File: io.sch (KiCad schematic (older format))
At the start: 12 parts, among them X1 CON-JST_SM04B-SRSS-TB, X2 CON-JST_SM04B-SRSS-TB, X3 CON-JST_SM04B-SRSS-TB, X4 CON-JST_SM04B-SRSS-TB, X5 CON-JST_SM04B-SRSS-TB, X6 CON-JST_SM04B-SRSS-TB, X7 CON-JST_SM04B-SRSS-TB, X8 CON-JST_SM04B-SRSS-TB

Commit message: added lots of stuff
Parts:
- added R8: 2k, Resistors_SMD:R_0402, symbol R
- R4: value 0R -> 10k
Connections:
- net GND: now also R8.2
- net TX2/ADC123_IN2: now also R8.1
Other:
- moved on the sheet: R4
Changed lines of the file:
@@
 EESchema Schematic File Version 2
+LIBS:stm32f4_lqfp64_mpu6050-rescue
 LIBS:power
 LIBS:device
@@
 LIBS:minimal
 LIBS:alis_parts
+LIBS:sensors
+LIBS:stm32
 LIBS:stm32f4_lqfp64_mpu6050-cache
 EELAYER 25 0
@@
 $Descr A4 11693 8268
 encoding utf-8
-Sheet 2 7
+Sheet 2 10
 Title ""
 Date ""
@@
 $EndComp
 $Comp
-L GND #PWR6
+L GND #PWR20
 U 1 1 5699735E
 P 7650 3350
-F 0 "#PWR6" H 7650 3100 50  0001 C CNN
+F 0 "#PWR20" H 7650 3100 50  0001 C CNN
 F 1 "GND" H 7658 3176 50  0000 C CNN
 F 2 "" H 7650 3350 50  0000 C CNN
@@
 TX5
 $Comp
-L GND #PWR4
+L GND #PWR9
 U 1 1 56997382
 P 4800 2850
-F 0 "#PWR4" H 4800 2600 50  0001 C CNN
+F 0 "#PWR9" H 4800 2600 50  0001 C CNN
 F 1 "GND" H 4808 2676 50  0000 C CNN
 F 2 "" H 4800 2850 50  0000 C CNN
@@
 TX4
 $Comp
-L GND #PWR8
+L GND #PWR26
 U 1 1 569973A7
 P 6300 4050
-F 0 "#PWR8" H 6300 3800 50  0001 C CNN
+F 0 "#PWR26" H 6300 3800 50  0001 C CNN
 F 1 "GND" H 6308 3876 50  0000 C CNN
 F 2 "" H 6300 4050 50  0000 C CNN
@@
 TX3
 $Comp
-L GND #PWR7
+L GND #PWR25
 U 1 1 569973CC
 P 3500 4050
-F 0 "#PWR7" H 3500 3800 50  0001 C CNN
+F 0 "#PWR25" H 3500 3800 50  0001 C CNN
 F 1 "GND" H 3508 3876 50  0000 C CNN
 F 2 "" H 3500 4050 50  0000 C CNN
@@
 $EndComp
 $Comp
-L GND #PWR5
+L GND #PWR10
 U 1 1 569973EE
 P 6350 2850
-F 0 "#PWR5" H 6350 2600 50  0001 C CNN
+F 0 "#PWR10" H 6350 2600 50  0001 C CNN
 F 1 "GND" H 6358 2676 50  0000 C CNN
 F 2 "" H 6350 2850 50  0000 C CNN
@@
 TX1
 $Comp
-L GND #PWR3
+L GND #PWR8
 U 1 1 56997413
 P 3500 2850
-F 0 "#PWR3" H 3500 2600 50  0001 C CNN
+F 0 "#PWR8" H 3500 2600 50  0001 C CNN
 F 1 "GND" H 3508 2676 50  0000 C CNN
 F 2 "" H 3500 2850 50  0000 C CNN
@@
 $EndComp
 $Comp
-L GND #PWR2
+L GND #PWR4
 U 1 1 569B0BD9
 P 3550 2100
-F 0 "#PWR2" H 3550 1850 50  0001 C CNN
+F 0 "#PWR4" H 3550 1850 50  0001 C CNN
 F 1 "GND" H 3558 1926 50  0000 C CNN
 F 2 "" H 3550 2100 50  0000 C CNN
@@
 L R R4
 U 1 1 569BB569
-P 7150 1950
-F 0 "R4" H 7220 1996 50  0000 L CNN
-F 1 "0R" H 7220 1904 50  0000 L CNN
-F 2 "Resistors_SMD:R_0402" V 7080 1950 50  0001 C CNN
-F 3 "" H 7150 1950 50  0000 C CNN
-	1    7150 1950
-	0    1    1    0
-$EndComp
-Text GLabel 7000 1950 0    60   Input ~ 0
+P 7050 1400
+F 0 "R4" H 7120 1446 50  0000 L CNN
+F 1 "10k" H 7120 1354 50  0000 L CNN
+F 2 "Resistors_SMD:R_0402" V 6980 1400 50  0001 C CNN
+F 3 "" H 7050 1400 50  0000 C CNN
+	1    7050 1400
+	1    0    0    -1
+$EndComp
+Text GLabel 7200 1600 2    60   Input ~ 0
 TX2/ADC123_IN2
-Text GLabel 7300 1950 2    60   Input ~ 0
+Text GLabel 7050 1100 0    60   Input ~ 0
 VCCEXT
+$Comp
+L R R8
+U 1 1 569D6AA2
+P 7050 1800
+F 0 "R8" H 7120 1846 50  0000 L CNN
+F 1 "2k" H 7120 1754 50  0000 L CNN
+F 2 "Resistors_SMD:R_0402" V 6980 1800 50  0001 C CNN
+F 3 "" H 7050 1800 50  0000 C CNN
+	1    7050 1800
+	1    0    0    -1
+$EndComp
+$Comp
+L GND #PWR5
+U 1 1 569D6B3D
+P 7050 2100
+F 0 "#PWR5" H 7050 1850 50  0001 C CNN
+F 1 "GND" H 7058 1926 50  0000 C CNN
+F 2 "" H 7050 2100 50  0000 C CNN
+F 3 "" H 7050 2100 50  0000 C CNN
+	1    7050 2100
+	1    0    0    -1
+$EndComp
+Wire Wire Line
+	7050 1100 7050 1250
+Wire Wire Line
+	7050 1550 7050 1650
+Wire Wire Line
+	7200 1600 7050 1600
+Connection ~ 7050 1600
+Wire Wire Line
+	7050 1950 7050 2100
 $EndSCHEMATC

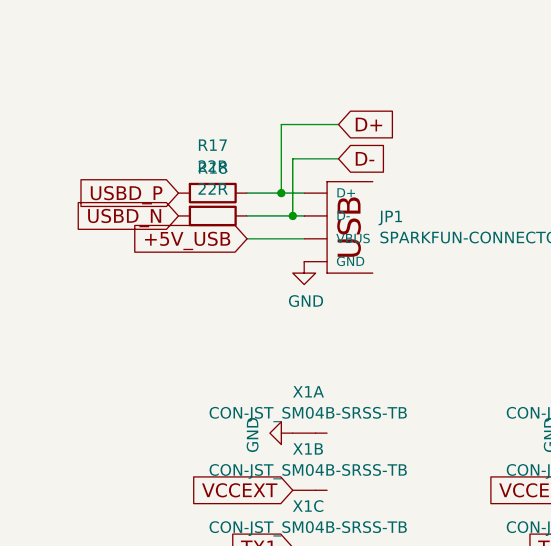
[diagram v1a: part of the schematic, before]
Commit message: added IMU int and USB sense in schematic
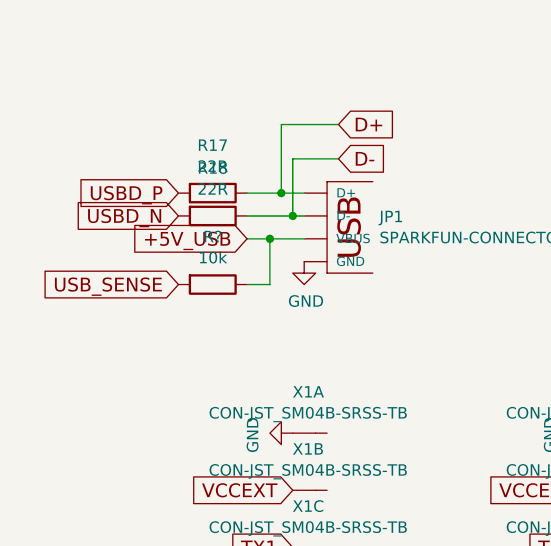
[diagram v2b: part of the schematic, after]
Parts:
- added R?: 10k, Resistors_SMD:R_0402, symbol R
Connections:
- net +5V_USB: now also R?.1
- new net USB_SENSE: R?.2
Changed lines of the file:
@@
 Wire Wire Line
 	7050 1950 7050 2100
+$Comp
+L R R?
+U 1 1 57056D51
+P 3150 2200
+F 0 "R?" V 2942 2200 50  0000 C CNN
+F 1 "10k" V 3034 2200 50  0000 C CNN
+F 2 "Resistors_SMD:R_0402" V 3080 2200 50  0001 C CNN
+F 3 "" H 3150 2200 50  0000 C CNN
+	1    3150 2200
+	0    1    1    0
+$EndComp
+Wire Wire Line
+	3300 2200 3400 2200
+Wire Wire Line
+	3400 2200 3400 2000
+Connection ~ 3400 2000
+Text GLabel 3000 2200 0    60   Input ~ 0
+USB_SENSE
 $EndSCHEMATC

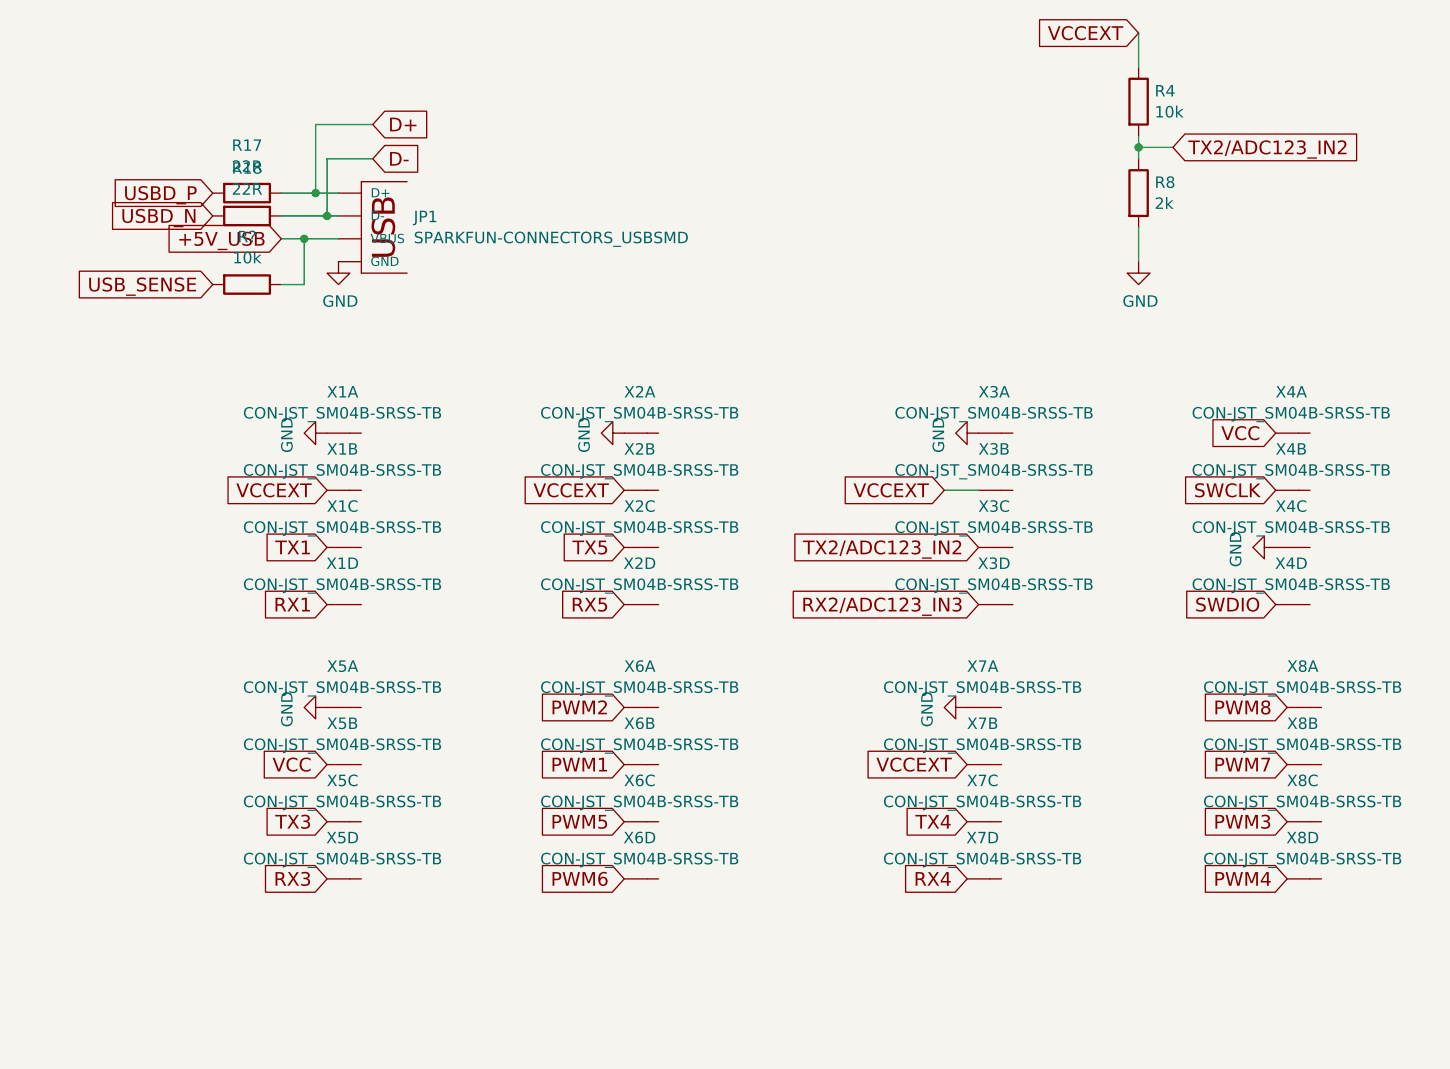
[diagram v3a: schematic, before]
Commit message: changed some netnames
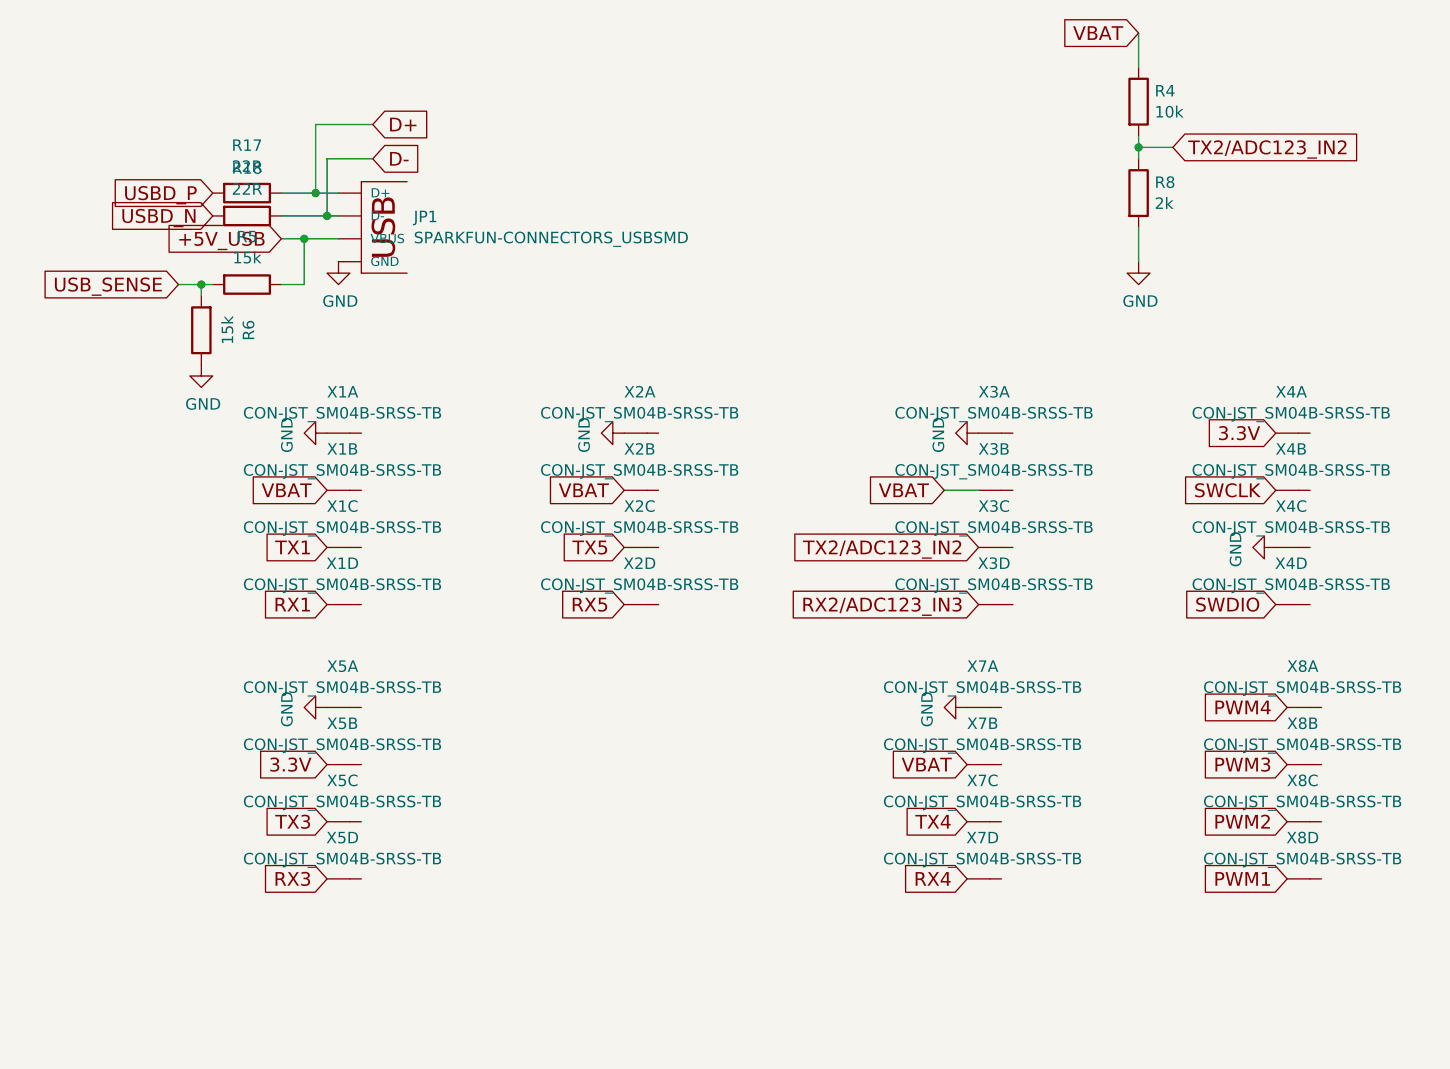
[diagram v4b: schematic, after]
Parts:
- removed X6: CON-JST_SM04B-SRSS-TB, Connectors_JST_SH:Connectors_JST_SM04B-SRSS-TB, symbol CON-JST_SM04B-SRSS-TB
- added R6: 15k, Resistors_SMD:R_0402, symbol R
- R5: renamed from R?; value 10k -> 15k
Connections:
- net PWM7 is gone; now on net PWM3: X8.2 (S)
- net PWM8 is gone; now on net PWM4: X8.1 (S)
- net GND: now also R6.1
- net PWM1: now also X8.4 (S)
- net PWM2: now also X8.3 (S)
- net PWM3: no longer X8.3 (S)
- net PWM4: no longer X8.4 (S)
- net USB_SENSE: now also R6.2
- net VCC renamed 3.3V
- net VCCEXT renamed VBAT
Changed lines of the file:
@@
 RX2/ADC123_IN3
 Text GLabel 3500 4300 0    60   Input ~ 0
-VCC
+3.3V
 Wire Wire Line
 	6200 3100 6350 3100
 Text GLabel 7700 4800 0    60   Input ~ 0
+PWM1
+Text GLabel 7700 4550 0    60   Input ~ 0
+PWM2
+Text GLabel 7700 4050 0    60   Input ~ 0
 PWM4
-Text GLabel 7700 4550 0    60   Input ~ 0
+Text GLabel 7700 4300 0    60   Input ~ 0
 PWM3
-Text GLabel 7700 4050 0    60   Input ~ 0
-PWM8
-Text GLabel 7700 4300 0    60   Input ~ 0
-PWM7
-Text GLabel 4800 4800 0    60   Input ~ 0
-PWM6
-Text GLabel 4800 4550 0    60   Input ~ 0
-PWM5
-Text GLabel 4800 4050 0    60   Input ~ 0
-PWM2
-Text GLabel 4800 4300 0    60   Input ~ 0
-PWM1
 Text GLabel 7650 3600 0    60   Input ~ 0
 SWDIO
@@
 SWCLK
 Text GLabel 7650 2850 0    60   Input ~ 0
-VCC
+3.3V
 $Comp
 L CON-JST_SM04B-SRSS-TB X?
@@
 $EndComp
 $Comp
-L CON-JST_SM04B-SRSS-TB X?
-U 4 1 56997342
-P 4900 4800
-AR Path="/56997342" Ref="X?"  Part="4"
-AR Path="/569801F2/56997342" Ref="X6"  Part="4"
-F 0 "X6" H 4868 4979 50  0000 C CNN
-F 1 "CON-JST_SM04B-SRSS-TB" H 4868 4887 50  0000 C CNN
-F 2 "Connectors_JST_SH:Connectors_JST_SM04B-SRSS-TB" H 4930 4950 20  0001 C CNN
-F 3 "" H 4900 4800 60  0000 C CNN
-	4    4900 4800
-	1    0    0    -1
-$EndComp
-$Comp
-L CON-JST_SM04B-SRSS-TB X?
-U 3 1 56997349
-P 4900 4550
-AR Path="/56997349" Ref="X?"  Part="3"
-AR Path="/569801F2/56997349" Ref="X6"  Part="3"
-F 0 "X6" H 4868 4729 50  0000 C CNN
-F 1 "CON-JST_SM04B-SRSS-TB" H 4868 4637 50  0000 C CNN
-F 2 "Connectors_JST_SH:Connectors_JST_SM04B-SRSS-TB" H 4930 4700 20  0001 C CNN
-F 3 "" H 4900 4550 60  0000 C CNN
-	3    4900 4550
-	1    0    0    -1
-$EndComp
-$Comp
-L CON-JST_SM04B-SRSS-TB X?
-U 2 1 56997350
-P 4900 4300
-AR Path="/56997350" Ref="X?"  Part="2"
-AR Path="/569801F2/56997350" Ref="X6"  Part="2"
-F 0 "X6" H 4868 4479 50  0000 C CNN
-F 1 "CON-JST_SM04B-SRSS-TB" H 4868 4387 50  0000 C CNN
-F 2 "Connectors_JST_SH:Connectors_JST_SM04B-SRSS-TB" H 4930 4450 20  0001 C CNN
-F 3 "" H 4900 4300 60  0000 C CNN
-	2    4900 4300
-	1    0    0    -1
-$EndComp
-$Comp
-L CON-JST_SM04B-SRSS-TB X?
-U 1 1 56997357
-P 4900 4050
-AR Path="/56997357" Ref="X?"  Part="1"
-AR Path="/569801F2/56997357" Ref="X6"  Part="1"
-F 0 "X6" H 4868 4229 50  0000 C CNN
-F 1 "CON-JST_SM04B-SRSS-TB" H 4868 4137 50  0000 C CNN
-F 2 "Connectors_JST_SH:Connectors_JST_SM04B-SRSS-TB" H 4930 4200 20  0001 C CNN
-F 3 "" H 4900 4050 60  0000 C CNN
-	1    4900 4050
-	1    0    0    -1
-$EndComp
-$Comp
-L GND #PWR20
+L GND #PWR01
 U 1 1 5699735E
 P 7650 3350
-F 0 "#PWR20" H 7650 3100 50  0001 C CNN
+F 0 "#PWR01" H 7650 3100 50  0001 C CNN
 F 1 "GND" H 7658 3176 50  0000 C CNN
 F 2 "" H 7650 3350 50  0000 C CNN
@@
 TX5
 $Comp
-L GND #PWR9
+L GND #PWR02
 U 1 1 56997382
 P 4800 2850
-F 0 "#PWR9" H 4800 2600 50  0001 C CNN
+F 0 "#PWR02" H 4800 2600 50  0001 C CNN
 F 1 "GND" H 4808 2676 50  0000 C CNN
 F 2 "" H 4800 2850 50  0000 C CNN
@@
 $EndComp
 Text GLabel 4800 3100 0    60   Input ~ 0
-VCCEXT
+VBAT
 $Comp
 L CON-JST_SM04B-SRSS-TB X?
@@
 TX4
 $Comp
-L GND #PWR26
+L GND #PWR03
 U 1 1 569973A7
 P 6300 4050
-F 0 "#PWR26" H 6300 3800 50  0001 C CNN
+F 0 "#PWR03" H 6300 3800 50  0001 C CNN
 F 1 "GND" H 6308 3876 50  0000 C CNN
 F 2 "" H 6300 4050 50  0000 C CNN
@@
 $EndComp
 Text GLabel 6300 4300 0    60   Input ~ 0
-VCCEXT
+VBAT
 $Comp
 L CON-JST_SM04B-SRSS-TB X?
@@
 TX3
 $Comp
-L GND #PWR25
+L GND #PWR04
 U 1 1 569973CC
 P 3500 4050
-F 0 "#PWR25" H 3500 3800 50  0001 C CNN
+F 0 "#PWR04" H 3500 3800 50  0001 C CNN
 F 1 "GND" H 3508 3876 50  0000 C CNN
 F 2 "" H 3500 4050 50  0000 C CNN
@@
 $EndComp
 $Comp
-L GND #PWR10
+L GND #PWR05
 U 1 1 569973EE
 P 6350 2850
-F 0 "#PWR10" H 6350 2600 50  0001 C CNN
+F 0 "#PWR05" H 6350 2600 50  0001 C CNN
 F 1 "GND" H 6358 2676 50  0000 C CNN
 F 2 "" H 6350 2850 50  0000 C CNN
@@
 $EndComp
 Text GLabel 6200 3100 0    60   Input ~ 0
-VCCEXT
+VBAT
 $Comp
 L CON-JST_SM04B-SRSS-TB X?
@@
 TX1
 $Comp
-L GND #PWR8
+L GND #PWR06
 U 1 1 56997413
 P 3500 2850
-F 0 "#PWR8" H 3500 2600 50  0001 C CNN
+F 0 "#PWR06" H 3500 2600 50  0001 C CNN
 F 1 "GND" H 3508 2676 50  0000 C CNN
 F 2 "" H 3500 2850 50  0000 C CNN
@@
 $EndComp
 Text GLabel 3500 3100 0    60   Input ~ 0
-VCCEXT
+VBAT
 $Comp
 L CON-JST_SM04B-SRSS-TB X?
@@
 $EndComp
 $Comp
-L GND #PWR4
+L GND #PWR07
 U 1 1 569B0BD9
 P 3550 2100
-F 0 "#PWR4" H 3550 1850 50  0001 C CNN
+F 0 "#PWR07" H 3550 1850 50  0001 C CNN
 F 1 "GND" H 3558 1926 50  0000 C CNN
 F 2 "" H 3550 2100 50  0000 C CNN
@@
 TX2/ADC123_IN2
 Text GLabel 7050 1100 0    60   Input ~ 0
-VCCEXT
+VBAT
 $Comp
 L R R8
@@
 $EndComp
 $Comp
-L GND #PWR5
+L GND #PWR08
 U 1 1 569D6B3D
 P 7050 2100
-F 0 "#PWR5" H 7050 1850 50  0001 C CNN
+F 0 "#PWR08" H 7050 1850 50  0001 C CNN
 F 1 "GND" H 7058 1926 50  0000 C CNN
 F 2 "" H 7050 2100 50  0000 C CNN
@@
 	7050 1950 7050 2100
 $Comp
-L R R?
+L R R5
 U 1 1 57056D51
 P 3150 2200
-F 0 "R?" V 2942 2200 50  0000 C CNN
-F 1 "10k" V 3034 2200 50  0000 C CNN
+F 0 "R5" V 2942 2200 50  0000 C CNN
+F 1 "15k" V 3034 2200 50  0000 C CNN
 F 2 "Resistors_SMD:R_0402" V 3080 2200 50  0001 C CNN
 F 3 "" H 3150 2200 50  0000 C CNN
@@
 	3400 2200 3400 2000
 Connection ~ 3400 2000
-Text GLabel 3000 2200 0    60   Input ~ 0
+Text GLabel 2850 2200 0    60   Input ~ 0
 USB_SENSE
+$Comp
+L R R6
+U 1 1 570A41D6
+P 2950 2400
+F 0 "R6" V 2742 2400 50  0000 C CNN
+F 1 "15k" V 2834 2400 50  0000 C CNN
+F 2 "Resistors_SMD:R_0402" V 2880 2400 50  0001 C CNN
+F 3 "" H 2950 2400 50  0000 C CNN
+	1    2950 2400
+	-1   0    0    1
+$EndComp
+$Comp
+L GND #PWR09
+U 1 1 570A4311
+P 2950 2550
+F 0 "#PWR09" H 2950 2300 50  0001 C CNN
+F 1 "GND" H 2958 2376 50  0000 C CNN
+F 2 "" H 2950 2550 50  0000 C CNN
+F 3 "" H 2950 2550 50  0000 C CNN
+	1    2950 2550
+	1    0    0    -1
+$EndComp
+Wire Wire Line
+	2850 2200 3000 2200
+Wire Wire Line
+	2950 2250 2950 2200
+Connection ~ 2950 2200
 $EndSCHEMATC

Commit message: OSD running on breadboard
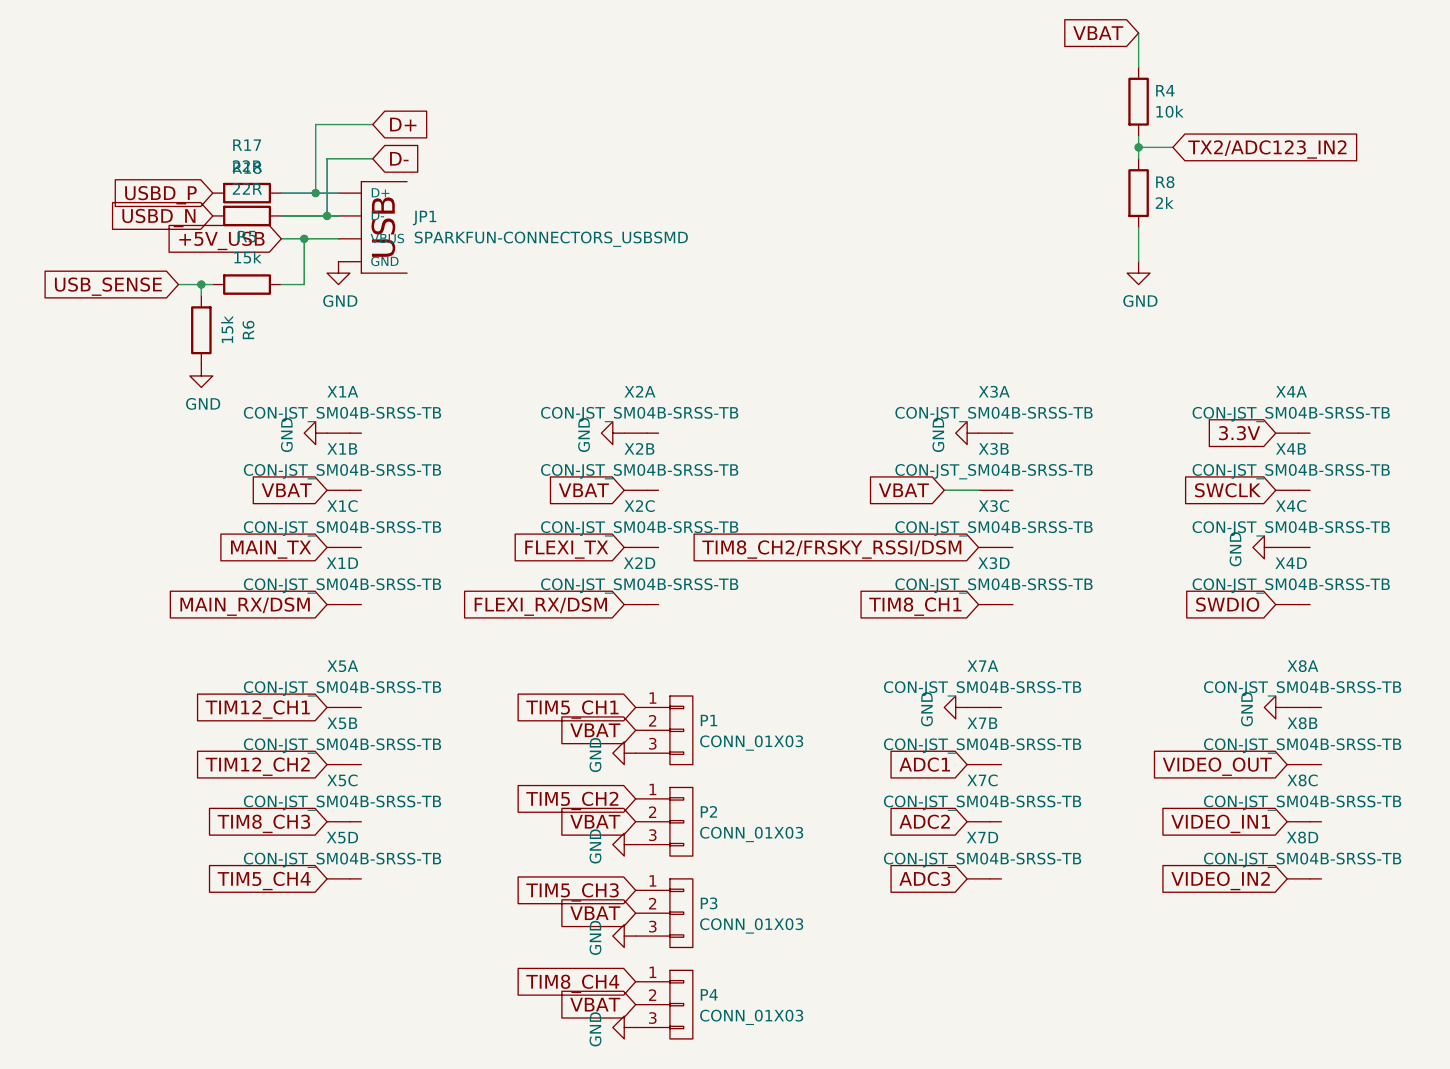
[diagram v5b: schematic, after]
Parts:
- added P1, P2, P3, P4: CONN_01X03, Pin_Headers:Pin_Header_Angled_1x03, symbol CONN_01X03
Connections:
- net PWM4 is gone; now on net GND: X8.1 (S)
- net 3.3V: no longer X5.2 (S)
- net GND: now also P1.3 (P3), P2.3 (P3), P3.3 (P3), P4.3 (P3); no longer X5.1 (S)
- net TX2/ADC123_IN2: no longer X3.3 (S)
- net VBAT: now also P1.2 (P2), P2.2 (P2), P3.2 (P2), P4.2 (P2); no longer X7.2 (S)
- net PWM1 renamed VIDEO_IN2
- net PWM2 renamed VIDEO_IN1
- net PWM3 renamed VIDEO_OUT
- net RX1 renamed MAIN_RX/DSM
- net RX2/ADC123_IN3 renamed TIM8_CH1
- net RX3 renamed TIM5_CH4
- net RX4 renamed ADC3
- net RX5 renamed FLEXI_RX/DSM
- net TX1 renamed MAIN_TX
- net TX3 renamed TIM8_CH3
- net TX4 renamed ADC2
- net TX5 renamed FLEXI_TX
- new net ADC1: X7.2 (S)
- new net TIM12_CH1: X5.1 (S)
- new net TIM12_CH2: X5.2 (S)
- new net TIM5_CH1: P1.1 (P1)
- new net TIM5_CH2: P2.1 (P1)
- new net TIM5_CH3: P3.1 (P1)
- new net TIM8_CH2/FRSKY_RSSI/DSM: X3.3 (S)
- new net TIM8_CH4: P4.1 (P1)
